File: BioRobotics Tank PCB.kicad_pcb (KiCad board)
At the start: 2 copper layers, 72 x 90 mm, 71 parts, among them J1 Conn_01x02, J2 Conn_01x02, J3 Conn_01x02, J4 Conn_01x02, J5 Conn_01x02, J6 Conn_01x02, J7 Conn_01x02, J8 Conn_02x05_Odd_Even, J9 Conn_01x05, Q1 IPD060N03LGATMA1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

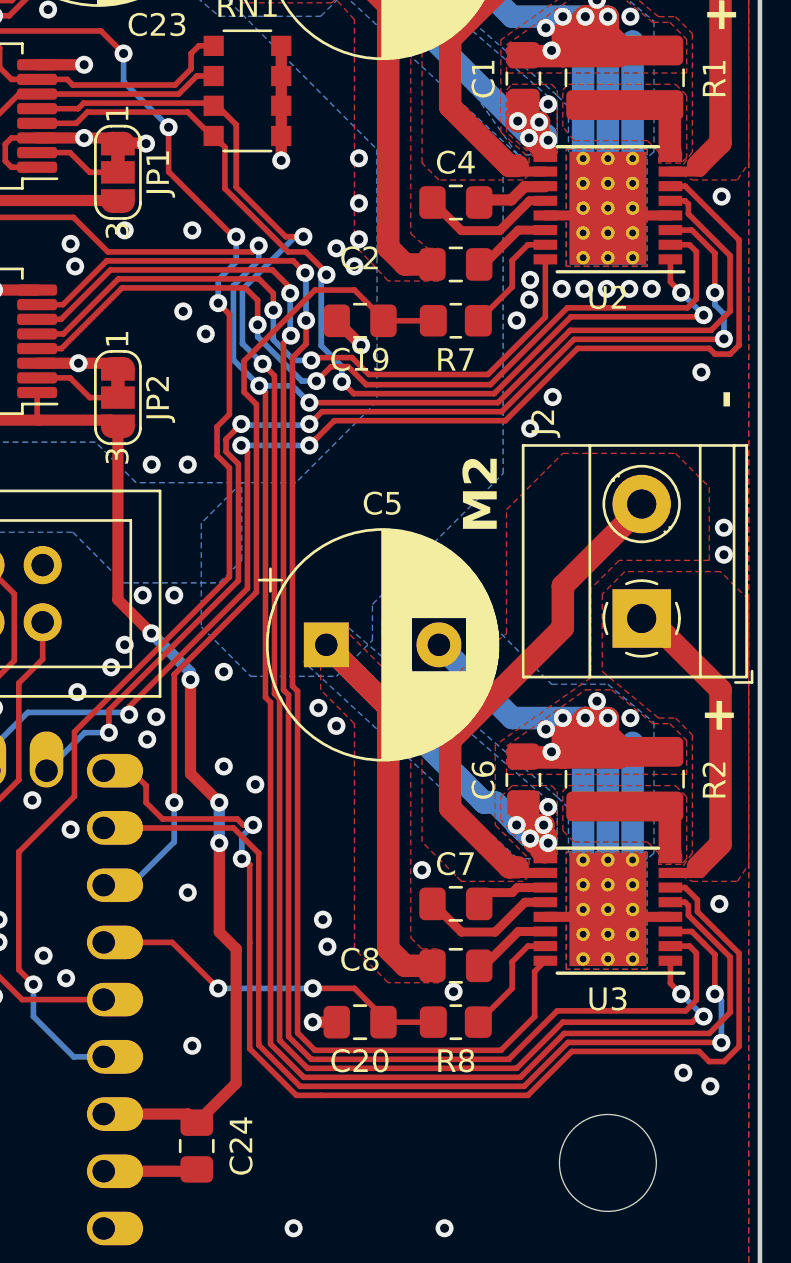
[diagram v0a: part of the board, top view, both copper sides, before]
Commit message: Add 10k pulldown to nSleep and export BOM
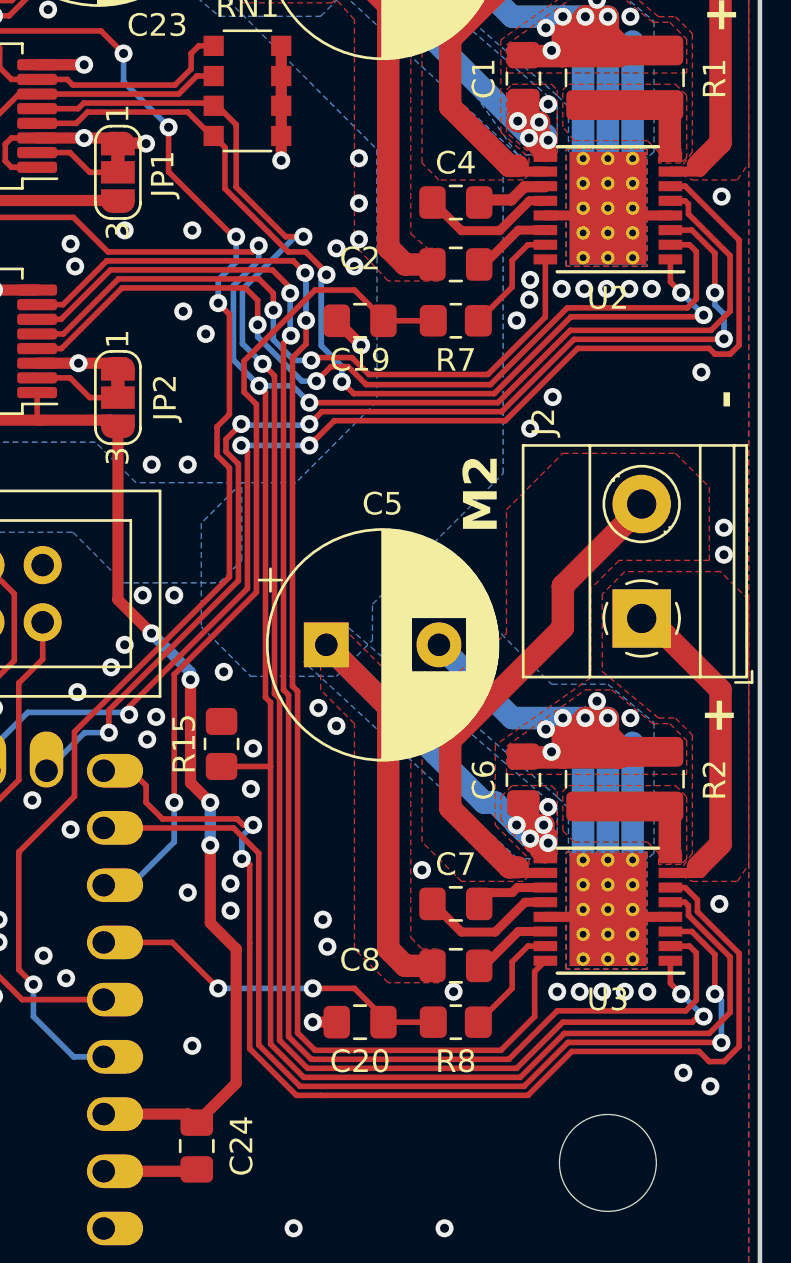
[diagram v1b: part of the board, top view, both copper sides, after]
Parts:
- added R15: 10k, Resistor_SMD:R_0805_2012Metric_Pad1.20x1.40mm_HandSolder, F.Cu at (168.1, 126.4)
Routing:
- net /~{M_SLEEP}: track 215.6 -> 217.8 mm
- net GND1: vias 237 -> 244

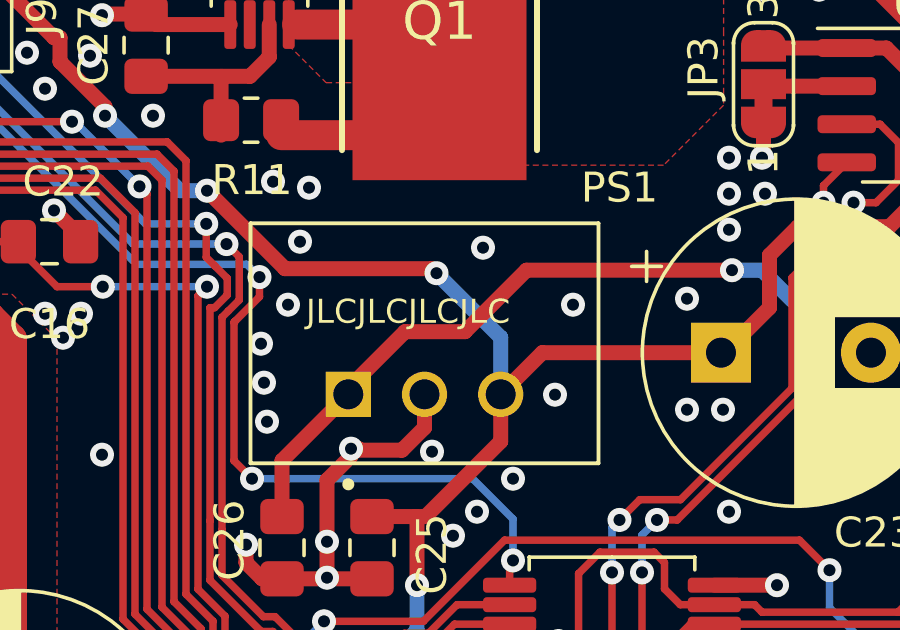
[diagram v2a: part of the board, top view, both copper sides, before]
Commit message: Change to product number to PCBWays template
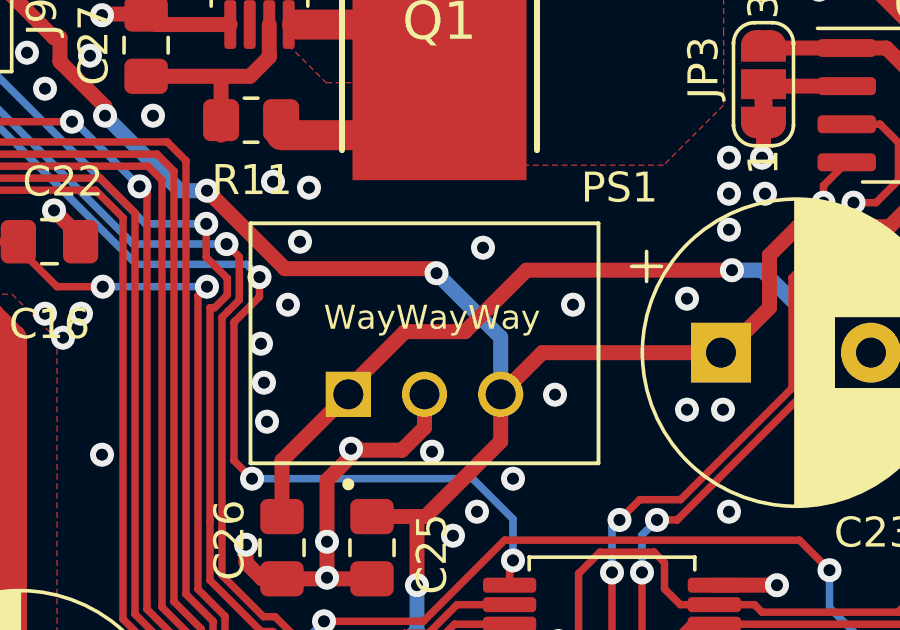
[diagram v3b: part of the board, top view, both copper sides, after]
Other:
- board text added: "WayWayWay"
- board text removed: "JLCJLCJLCJLC"
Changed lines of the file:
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@@
     (effects (font (size 1.5 1.5) (thickness 0.2) bold) (justify bottom))
   )
-  (gr_text "JLCJLCJLCJLC" (at 146.3 87.6) (layer "F.SilkS")
-    (effects (font (size 0.8 0.8) (thickness 0.1875)) (justify left bottom))
+  (gr_text "WayWayWay" (at 150.5 87.8) (layer "F.SilkS")
+    (effects (font (size 0.8 0.8) (thickness 0.1875)) (justify bottom))
   )
   (gr_text "-" (at 167.9 61 180) (layer "F.SilkS" knockout)
